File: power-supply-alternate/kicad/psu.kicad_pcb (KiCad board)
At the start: 2 copper layers, 23 x 22.1 mm, 16 parts, among them J3 SSQ-103-03-G-D, U1 MAX889TESA+, U3 TPS72301DBVR, U5 TPS79333DBVR

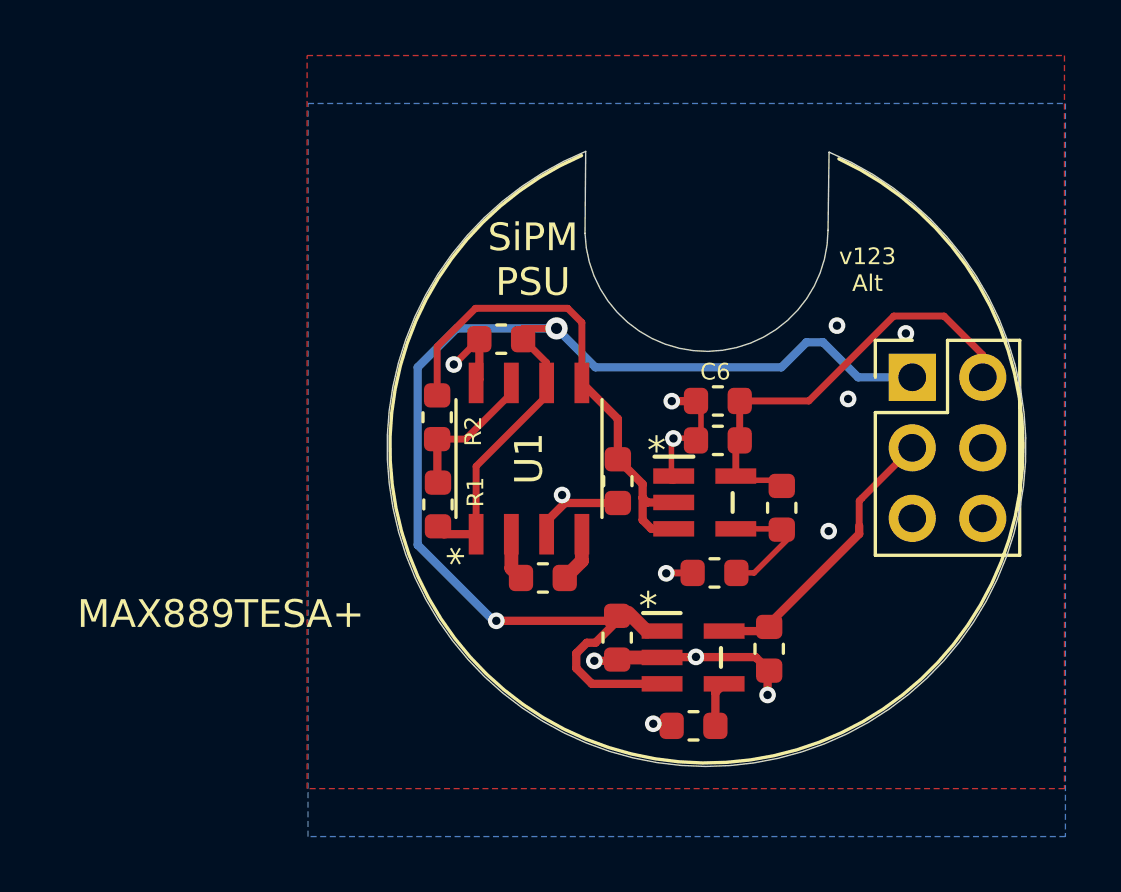
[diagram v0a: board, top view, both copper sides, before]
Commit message: Check in (tested) alternative psu
Can use easier to get parts for the charge pump and positive regulator.

Specs are actually better than the original design but the difference is insignificant.  We bumped the negative voltage rail up a little (-4.6V) due to better parts.

Can use the existing TPS79333 (which is hard to find) or the tps7a20 which has better specs and is pin compatible.  Can optionally use the 4.2 or 4.5v version as well to extend dynamic range, although this won't make a difference with the current bias generator and s14420 due to current limits.  Maybe help if used with other SiPMs.
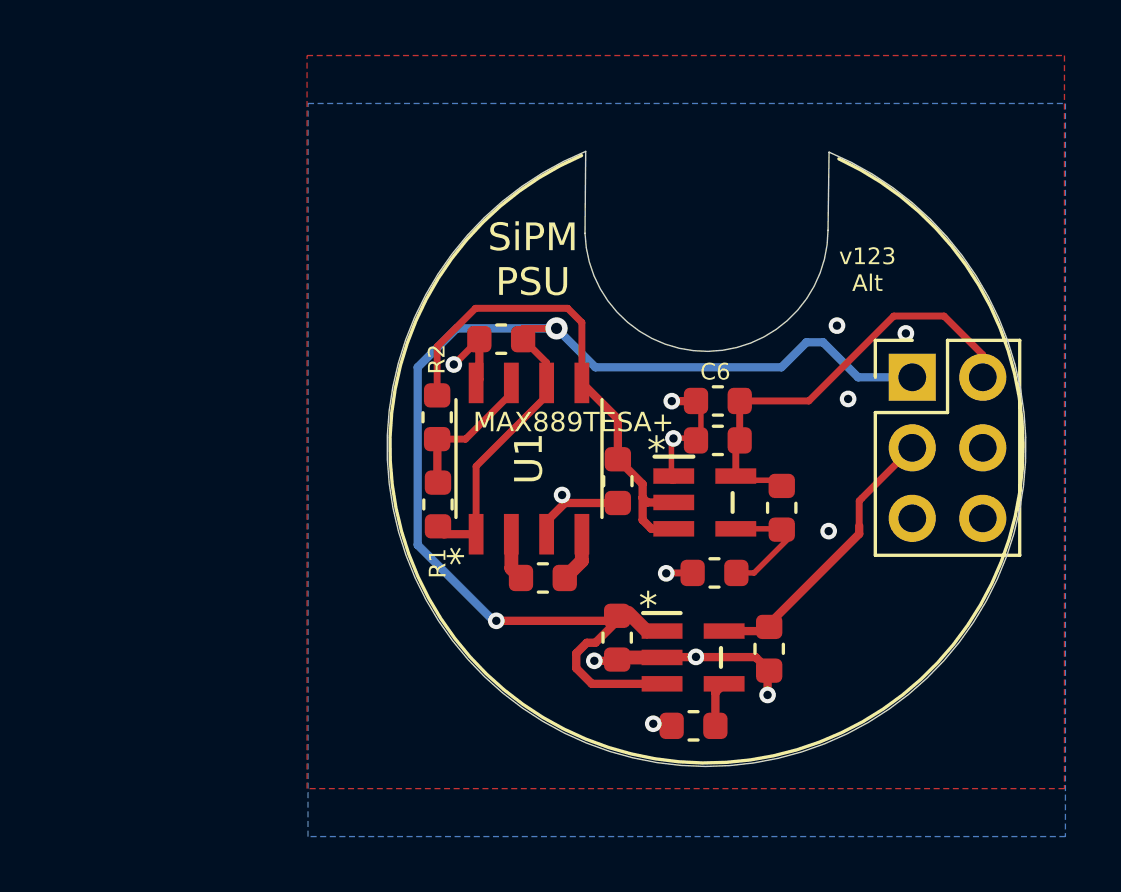
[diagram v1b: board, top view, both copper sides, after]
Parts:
- R8: value 64.9k -> 73.2k
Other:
- board text added: "-4.67V"
- board text removed: "-4.3V"
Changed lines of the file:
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@@
       (layerselection 0x00010f0_ffffffff)
       (disableapertmacros false)
-      (usegerberextensions false)
-      (usegerberattributes false)
+      (usegerberextensions true)
+      (usegerberattributes true)
       (usegerberadvancedattributes false)
       (creategerberjobfile false)
@@
       (plotinvisibletext false)
       (sketchpadsonfab false)
-      (subtractmaskfromsilk false)
+      (subtractmaskfromsilk true)
       (outputformat 1)
       (mirror false)
@@
   (net 8 "Net-(C17-Pad2)")
   (net 9 "Net-(R8-Pad1)")
-  (net 10 "Net-(U1-Pad7)")
+  (net 10 "Net-(R1-Pad1)")
   (footprint "footprints:C_0603_1608Metric" (layer "F.Cu")
     (at 199.53265 110.612501)
@@
       (effects (font (size 0.6 0.6) (thickness 0.1)))
     )
-    (fp_text value "64.9k" (at 0 1.43 90) (layer "F.Fab") hide
+    (fp_text value "73.2k" (at 0 1.43 90) (layer "F.Fab") hide
       (effects (font (size 1 1) (thickness 0.15)))
     )
@@
       (effects (font (size 1 1) (thickness 0.15)))
     )
-    (fp_text value "MAX889TESA+" (at -5.6 -11.1 180) (layer "F.SilkS")
-      (effects (font (size 1 1) (thickness 0.15)))
+    (fp_text value "MAX889TESA+" (at 1.3075 1.6026 180) (layer "F.SilkS")
+      (effects (font (size 0.7 0.7) (thickness 0.1)))
     )
     (fp_text user "*" (at -3.5125 -2.4074 90) (layer "F.SilkS")
@@
       (net 2 "+5V") (pinfunction "*SHDN") (pintype "input"))
     (pad "7" smd rect locked (at 2.72415 -0.635 90) (size 1.4605 0.5334) (layers "F.Cu" "F.Paste" "F.Mask")
-      (net 10 "Net-(U1-Pad7)") (pinfunction "FB") (pintype "input"))
+      (net 10 "Net-(R1-Pad1)") (pinfunction "FB") (pintype "input"))
     (pad "8" smd rect locked (at 2.72415 -1.905 90) (size 1.4605 0.5334) (layers "F.Cu" "F.Paste" "F.Mask")
       (net 1 "GND") (pinfunction "AGND") (pintype "power_in"))
@@
     (property "Sheetname" "")
     (attr smd)
-    (fp_text reference "R1" (at -0.4475 -1.3526 90) (layer "F.SilkS")
+    (fp_text reference "R1" (at 2.12 0.01 90) (layer "F.SilkS")
       (effects (font (size 0.6 0.6) (thickness 0.1)))
     )
@@
     (fp_line (start 0.8 -0.4) (end 0.8 0.4) (layer "F.Fab") (width 0.1))
     (pad "1" smd roundrect locked (at -0.7875 0 270) (size 0.875 0.95) (layers "F.Cu" "F.Paste" "F.Mask") (roundrect_rratio 0.25)
-      (net 10 "Net-(U1-Pad7)") (pintype "passive"))
+      (net 10 "Net-(R1-Pad1)") (pintype "passive"))
     (pad "2" smd roundrect locked (at 0.7875 0 270) (size 0.875 0.95) (layers "F.Cu" "F.Paste" "F.Mask") (roundrect_rratio 0.25)
       (net 2 "+5V") (pintype "passive"))
@@
     (property "Sheetname" "")
     (attr smd)
-    (fp_text reference "R2" (at 0.5 -1.3 90) (layer "F.SilkS")
+    (fp_text reference "R2" (at -2.09 0.01 90) (layer "F.SilkS")
       (effects (font (size 0.6 0.6) (thickness 0.1)))
     )
@@
       (net 4 "-5V") (pintype "passive"))
     (pad "2" smd roundrect locked (at 0.7875 0 270) (size 0.875 0.95) (layers "F.Cu" "F.Paste" "F.Mask") (roundrect_rratio 0.25)
-      (net 10 "Net-(U1-Pad7)") (pintype "passive"))
+      (net 10 "Net-(R1-Pad1)") (pintype "passive"))
     (model "${KIPRJMOD}/step/R_0603_1608Metric.step"
       (offset (xyz 0 0 0))
@@
     (effects (font (size 1 1) (thickness 0.15)) (justify mirror))
   )
-  (gr_text "-4.3V" (at 209.3 96.1) (layer "B.SilkS")
+  (gr_text "-4.67V" (at 208.94 96.09) (layer "B.SilkS")
     (effects (font (size 0.6 0.6) (thickness 0.15)) (justify mirror))
   )
